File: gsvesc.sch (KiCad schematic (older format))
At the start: 29 parts, among them J1 Conn_01x06, J13 Conn_01x02, J2 Conn_01x06, J3 Conn_01x06, J4 Conn_01x05, J5 Conn_01x03, J6 USB_B_Mini, J7 BAT+, J8 BAT-, U17 TMP100NA_250

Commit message: fertig gerouted
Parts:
- added R37, R40: R, Resistor_SMD:R_0805_2012Metric, symbol Device:R
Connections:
- net MCU/I2C1_SCL: now also R40.2
- net MCU/I2C1_SDA: now also R37.2
- net VCC: now also R37.1, R40.1
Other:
- moved on the sheet: U17
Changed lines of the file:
@@
 L gsvesc:TMP100NA_250 U17
 U 1 1 5EB0793D
-P 5250 4650
-F 0 "U17" H 6050 5137 60  0000 C CNN
-F 1 "TMP100NA_250" H 6050 5031 60  0000 C CNN
-F 2 "gsvesc:TMP100NA_250" H 6050 4990 60  0001 C CNN
-F 3 "" H 5250 4650 60  0000 C CNN
-	1    5250 4650
+P 7600 5500
+F 0 "U17" H 8400 5987 60  0000 C CNN
+F 1 "TMP100NA_250" H 8400 5881 60  0000 C CNN
+F 2 "gsvesc:TMP100NA_250" H 8400 5840 60  0001 C CNN
+F 3 "" H 7600 5500 60  0000 C CNN
+	1    7600 5500
 	1    0    0    -1
 $EndComp
-Wire Wire Line
-	4600 4600 4750 4600
-Wire Wire Line
-	4750 4600 4750 4450
-Wire Wire Line
-	4750 4450 5250 4450
-Wire Wire Line
-	4600 4700 4800 4700
-Wire Wire Line
-	4800 4700 4800 4550
-Wire Wire Line
-	4800 4550 5250 4550
 $Comp
 L power:VCC #PWR0159
 U 1 1 5EB10F14
-P 5250 4700
-F 0 "#PWR0159" H 5250 4550 50  0001 C CNN
-F 1 "VCC" V 5268 4827 50  0000 L CNN
-F 2 "" H 5250 4700 50  0001 C CNN
-F 3 "" H 5250 4700 50  0001 C CNN
-	1    5250 4700
+P 7600 5550
+F 0 "#PWR0159" H 7600 5400 50  0001 C CNN
+F 1 "VCC" V 7618 5677 50  0000 L CNN
+F 2 "" H 7600 5550 50  0001 C CNN
+F 3 "" H 7600 5550 50  0001 C CNN
+	1    7600 5550
 	0    -1   -1   0
 $EndComp
@@
 L power:GND #PWR0160
 U 1 1 5EB11007
-P 6400 4700
-F 0 "#PWR0160" H 6400 4450 50  0001 C CNN
-F 1 "GND" H 6405 4527 50  0000 C CNN
-F 2 "" H 6400 4700 50  0001 C CNN
-F 3 "" H 6400 4700 50  0001 C CNN
-	1    6400 4700
+P 8750 5550
+F 0 "#PWR0160" H 8750 5300 50  0001 C CNN
+F 1 "GND" H 8755 5377 50  0000 C CNN
+F 2 "" H 8750 5550 50  0001 C CNN
+F 3 "" H 8750 5550 50  0001 C CNN
+	1    8750 5550
 	1    0    0    -1
 $EndComp
+Wire Wire Line
+	6850 4700 6850 5400
+Wire Wire Line
+	7000 4600 7000 5300
+Wire Wire Line
+	7000 5300 7400 5300
+Wire Wire Line
+	4600 4700 6850 4700
+Wire Wire Line
+	4600 4600 7000 4600
+$Comp
+L Device:R R37
+U 1 1 5EB13175
+P 7150 5050
+F 0 "R37" H 7220 5096 50  0000 L CNN
+F 1 "R" H 7220 5005 50  0000 L CNN
+F 2 "Resistor_SMD:R_0805_2012Metric" V 7080 5050 50  0001 C CNN
+F 3 "~" H 7150 5050 50  0001 C CNN
+	1    7150 5050
+	1    0    0    -1
+$EndComp
+$Comp
+L Device:R R40
+U 1 1 5EB132CF
+P 7400 5050
+F 0 "R40" H 7470 5096 50  0000 L CNN
+F 1 "R" H 7470 5005 50  0000 L CNN
+F 2 "Resistor_SMD:R_0805_2012Metric" V 7330 5050 50  0001 C CNN
+F 3 "~" H 7400 5050 50  0001 C CNN
+	1    7400 5050
+	1    0    0    -1
+$EndComp
+Wire Wire Line
+	7400 5200 7400 5300
+Connection ~ 7400 5300
+Wire Wire Line
+	7400 5300 7600 5300
+Wire Wire Line
+	7150 5200 7150 5400
+Wire Wire Line
+	6850 5400 7150 5400
+Connection ~ 7150 5400
+Wire Wire Line
+	7150 5400 7600 5400
+Wire Wire Line
+	7150 4900 7150 4800
+Wire Wire Line
+	7150 4800 7400 4800
+Wire Wire Line
+	7400 4800 7400 4900
+$Comp
+L power:VCC #PWR0161
+U 1 1 5EB25A1D
+P 7150 4800
+F 0 "#PWR0161" H 7150 4650 50  0001 C CNN
+F 1 "VCC" V 7168 4927 50  0000 L CNN
+F 2 "" H 7150 4800 50  0001 C CNN
+F 3 "" H 7150 4800 50  0001 C CNN
+	1    7150 4800
+	1    0    0    -1
+$EndComp
+Connection ~ 7150 4800
 $EndSCHEMATC

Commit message: Ready for JLC
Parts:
- R37, R40: value R -> 10k0
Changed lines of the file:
@@
 P 7150 5050
 F 0 "R37" H 7220 5096 50  0000 L CNN
-F 1 "R" H 7220 5005 50  0000 L CNN
+F 1 "10k0" H 7220 5005 50  0000 L CNN
 F 2 "Resistor_SMD:R_0805_2012Metric" V 7080 5050 50  0001 C CNN
 F 3 "~" H 7150 5050 50  0001 C CNN
@@
 P 7400 5050
 F 0 "R40" H 7470 5096 50  0000 L CNN
-F 1 "R" H 7470 5005 50  0000 L CNN
+F 1 "10k0" H 7470 5005 50  0000 L CNN
 F 2 "Resistor_SMD:R_0805_2012Metric" V 7330 5050 50  0001 C CNN
 F 3 "~" H 7400 5050 50  0001 C CNN

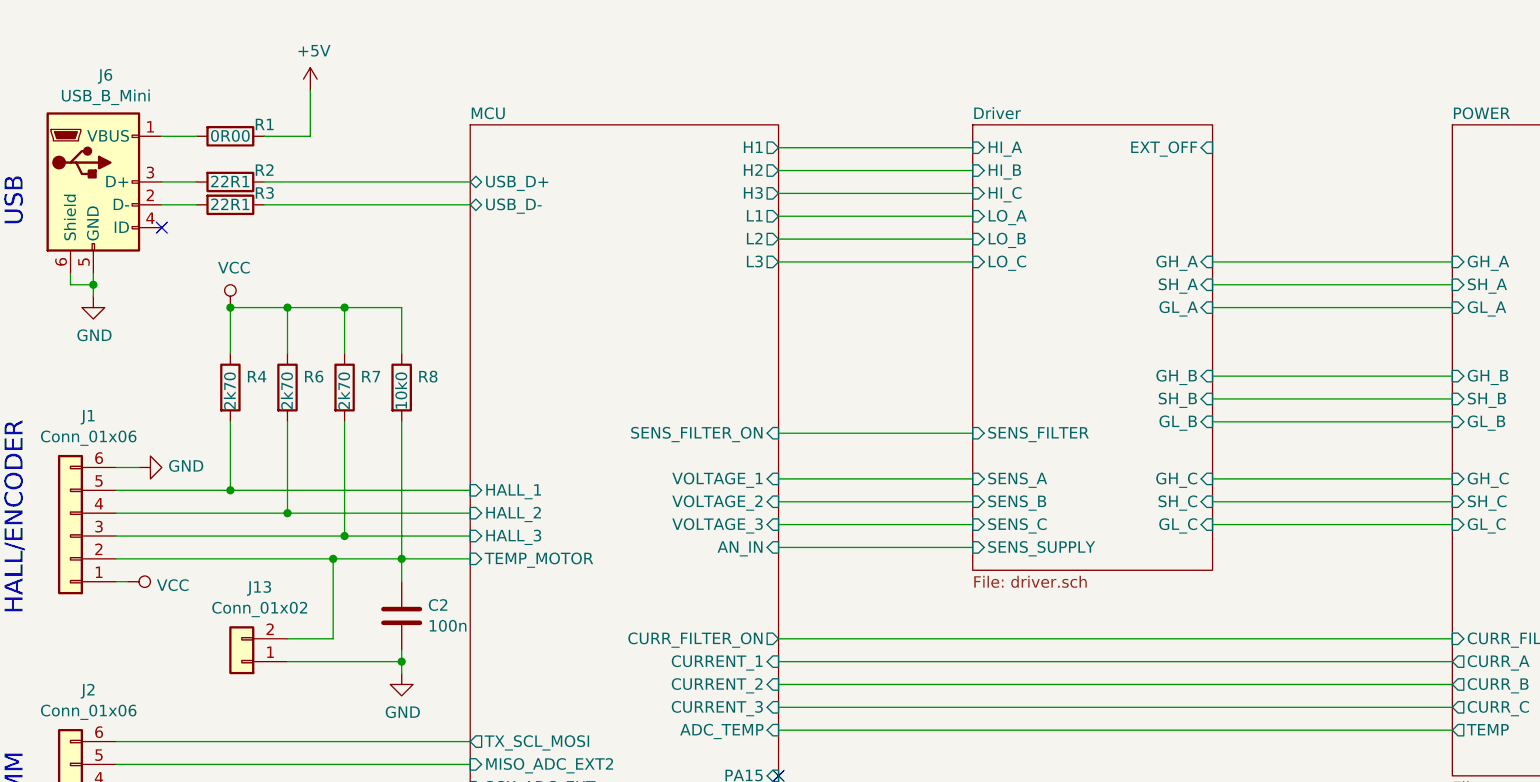
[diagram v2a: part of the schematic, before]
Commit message: some bug fixes for next pcb-run
- Add JST connector for Motor Temp
- Remove USB 5V
- add correct footprint for D8,9,10
- add JST connector for external off
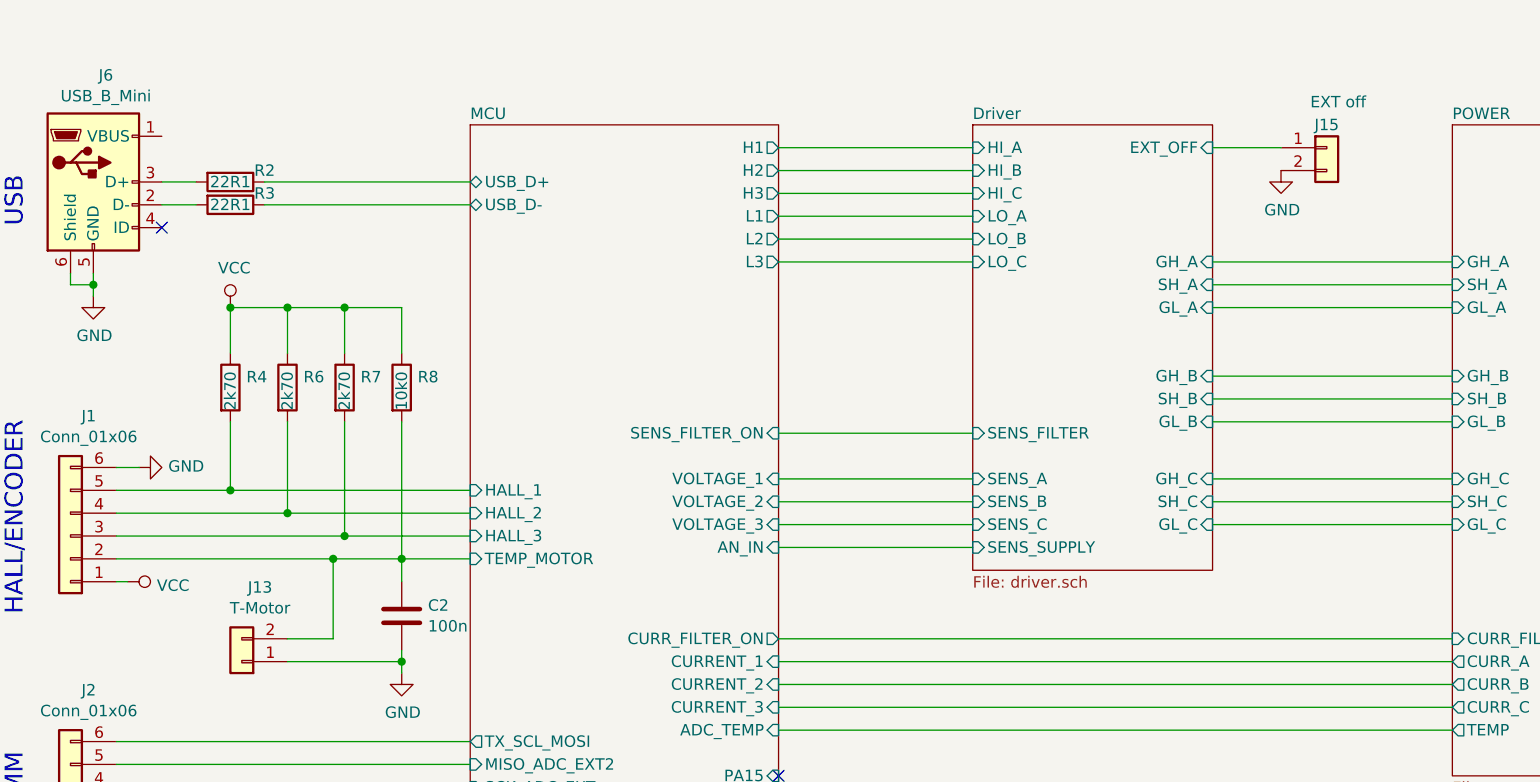
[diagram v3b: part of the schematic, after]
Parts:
- removed R1: 0R00, Resistor_SMD:R_0805_2012Metric, symbol Device:R
- added J15: EXT off, Connector_JST:JST_SH_BM02B-SRSS-TB_1x02-1MP_P1.00mm_Vertical, symbol Connector_Generic:Conn_01x02
- J13: value Conn_01x02 -> T-Motor; footprint gsvesc:2pad_smd_testpin -> Connector_JST:JST_SH_BM02B-SRSS-TB_1x02-1MP_P1.00mm_Vertical
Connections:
- net Driver/EXT_OFF: now also J15.1 (Pin_1)
- net GND: now also J15.2 (Pin_2)
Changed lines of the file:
@@
 	1600 2200 1600 2150
-$Comp
-L Device:R R1
-U 1 1 5BE878C2
-P 2200 1500
-F 0 "R1" V 2150 1650 50  0000 C CNN
-F 1 "0R00" V 2200 1500 50  0000 C CNN
-F 2 "Resistor_SMD:R_0805_2012Metric" V 2130 1500 50  0001 C CNN
-F 3 "~" H 2200 1500 50  0001 C CNN
-	1    2200 1500
-	0    1    1    0
-$EndComp
 $Comp
 L Device:R R2
@@
 	0    1    1    0
 $EndComp
-Wire Wire Line
-	1900 1500 2050 1500
-Wire Wire Line
-	2350 1500 2550 1500
-Wire Wire Line
-	2550 1500 2550 1300
 Wire Wire Line
 	1500 2100 1500 2150
@@
 F6 "GPIO3" I L 5200 5200 50
 $EndSheet
-$Comp
-L power:+5V #PWR013
-U 1 1 5BEB4C48
-P 2550 1300
-F 0 "#PWR013" H 2550 1150 50  0001 C CNN
-F 1 "+5V" H 2565 1473 50  0000 C CNN
-F 2 "" H 2550 1300 50  0001 C CNN
-F 3 "" H 2550 1300 50  0001 C CNN
-	1    2550 1300
-	1    0    0    -1
-$EndComp
 Wire Wire Line
 	4600 1550 5450 1550
@@
 P 2250 3800
 F 0 "J13" H 2170 3475 50  0000 C CNN
-F 1 "Conn_01x02" H 2170 3566 50  0000 C CNN
-F 2 "gsvesc:2pad_smd_testpin" H 2250 3800 50  0001 C CNN
+F 1 "T-Motor" H 2170 3566 50  0000 C CNN
+F 2 "Connector_JST:JST_SH_BM02B-SRSS-TB_1x02-1MP_P1.00mm_Vertical" H 2250 3800 50  0001 C CNN
 F 3 "~" H 2250 3800 50  0001 C CNN
 	1    2250 3800
@@
 $EndComp
 Connection ~ 7150 4800
+$Comp
+L Connector_Generic:Conn_01x02 J15
+U 1 1 5ECFB072
+P 7000 1550
+F 0 "J15" H 7000 1650 50  0000 C CNN
+F 1 "EXT off" H 7050 1750 50  0000 C CNN
+F 2 "Connector_JST:JST_SH_BM02B-SRSS-TB_1x02-1MP_P1.00mm_Vertical" H 7000 1550 50  0001 C CNN
+F 3 "~" H 7000 1550 50  0001 C CNN
+	1    7000 1550
+	1    0    0    -1
+$EndComp
+Wire Wire Line
+	6500 1550 6800 1550
+$Comp
+L power:GND #PWR0154
+U 1 1 5ECFFD27
+P 6800 1650
+F 0 "#PWR0154" H 6800 1400 50  0001 C CNN
+F 1 "GND" H 6805 1477 50  0000 C CNN
+F 2 "" H 6800 1650 50  0001 C CNN
+F 3 "" H 6800 1650 50  0001 C CNN
+	1    6800 1650
+	1    0    0    -1
+$EndComp
 $EndSCHEMATC

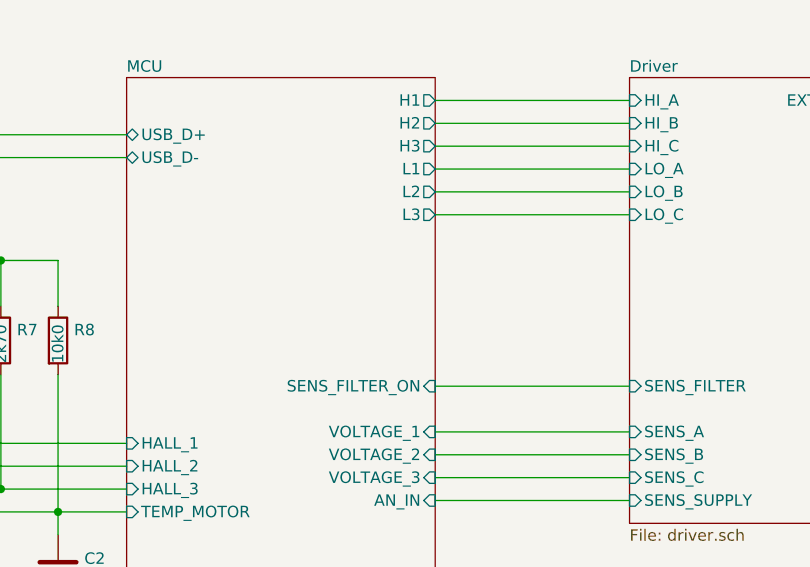
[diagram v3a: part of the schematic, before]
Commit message: BUG Fixes, see BUGS.txt
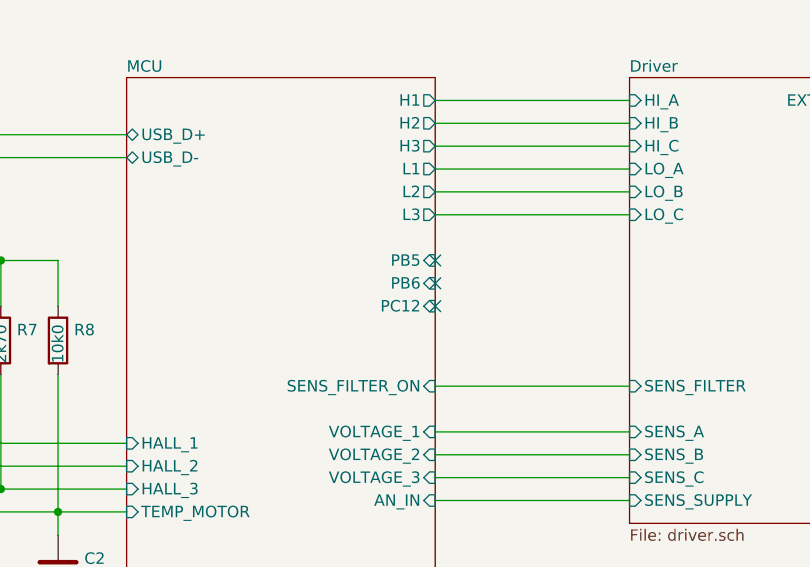
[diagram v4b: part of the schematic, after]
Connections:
- no-connect marks 3 -> 6
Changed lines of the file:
@@
 F45 "I2C1_SCL" I R 4600 4600 50
 F46 "I2C1_SDA" I R 4600 4700 50
+F47 "PB5" I R 4600 2250 50
+F48 "PB6" I R 4600 2350 50
+F49 "PC12" I R 4600 2450 50
 $EndSheet
 $Sheet
@@
 	1    0    0    -1
 $EndComp
+NoConn ~ 4600 2250
+NoConn ~ 4600 2350
+NoConn ~ 4600 2450
 $EndSCHEMATC

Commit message: bug fixing
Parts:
- removed J15: EXT off, Connector_JST:JST_SH_BM02B-SRSS-TB_1x02-1MP_P1.00mm_Vertical, symbol Connector_Generic:Conn_01x02
- added J15: EXT_OFF, Connector_JST:JST_SH_BM06B-SRSS-TB_1x06-1MP_P1.00mm_Vertical, symbol Connector_Generic:Conn_01x06
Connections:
- net +12V: now also J15.2 (Pin_2)
- net Driver/EXT_OFF: now also J15.4 (Pin_4)
- net GND: now also J15.6 (Pin_6)
- net VBAT: now also J15.1 (Pin_1)
- net VCC: now also J15.3 (Pin_3)
- new net Driver/EXT_OFF_DIRECT: J15.5 (Pin_5)
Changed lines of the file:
@@
 F21 "SENS_A" I L 5450 3000 50
 F22 "EXT_OFF" I R 6500 1550 50
+F23 "EXT_OFF_DIRECT" I R 6500 1650 50
 $EndSheet
 Wire Wire Line
@@
 Connection ~ 7150 4800
 $Comp
-L Connector_Generic:Conn_01x02 J15
-U 1 1 5ECFB072
-P 7000 1550
-F 0 "J15" H 7000 1650 50  0000 C CNN
-F 1 "EXT off" H 7050 1750 50  0000 C CNN
-F 2 "Connector_JST:JST_SH_BM02B-SRSS-TB_1x02-1MP_P1.00mm_Vertical" H 7000 1550 50  0001 C CNN
-F 3 "~" H 7000 1550 50  0001 C CNN
-	1    7000 1550
-	1    0    0    -1
-$EndComp
-Wire Wire Line
-	6500 1550 6800 1550
-$Comp
 L power:GND #PWR0154
 U 1 1 5ECFFD27
-P 6800 1650
-F 0 "#PWR0154" H 6800 1400 50  0001 C CNN
-F 1 "GND" H 6805 1477 50  0000 C CNN
-F 2 "" H 6800 1650 50  0001 C CNN
-F 3 "" H 6800 1650 50  0001 C CNN
-	1    6800 1650
+P 6950 1750
+F 0 "#PWR0154" H 6950 1500 50  0001 C CNN
+F 1 "GND" H 6955 1577 50  0000 C CNN
+F 2 "" H 6950 1750 50  0001 C CNN
+F 3 "" H 6950 1750 50  0001 C CNN
+	1    6950 1750
 	1    0    0    -1
 $EndComp
@@
 NoConn ~ 4600 2350
 NoConn ~ 4600 2450
+$Comp
+L power:VCC #PWR0162
+U 1 1 5ECFCDBF
+P 6950 1450
+F 0 "#PWR0162" H 6950 1300 50  0001 C CNN
+F 1 "VCC" V 6968 1577 50  0000 L CNN
+F 2 "" H 6950 1450 50  0001 C CNN
+F 3 "" H 6950 1450 50  0001 C CNN
+	1    6950 1450
+	0    -1   -1   0
+$EndComp
+Wire Wire Line
+	6500 1550 6950 1550
+$Comp
+L Connector_Generic:Conn_01x06 J15
+U 1 1 5ED44562
+P 7150 1450
+F 0 "J15" H 7100 1750 50  0000 C CNN
+F 1 "EXT_OFF" H 7150 1850 50  0000 C CNN
+F 2 "Connector_JST:JST_SH_BM06B-SRSS-TB_1x06-1MP_P1.00mm_Vertical" H 7150 1450 50  0001 C CNN
+F 3 "~" H 7150 1450 50  0001 C CNN
+	1    7150 1450
+	1    0    0    -1
+$EndComp
+Wire Wire Line
+	6500 1650 6950 1650
+$Comp
+L power:+12V #PWR0165
+U 1 1 5ED6AA00
+P 6950 1350
+F 0 "#PWR0165" H 6950 1200 50  0001 C CNN
+F 1 "+12V" V 6965 1478 50  0000 L CNN
+F 2 "" H 6950 1350 50  0001 C CNN
+F 3 "" H 6950 1350 50  0001 C CNN
+	1    6950 1350
+	0    -1   -1   0
+$EndComp
+Text GLabel 6950 1250 0    50   Input ~ 0
+VBAT
 $EndSCHEMATC

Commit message: add PDF
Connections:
- net Driver/EXT_OFF renamed Driver/EN_3V3
- net Driver/EXT_OFF_DIRECT renamed Driver/EN_12V
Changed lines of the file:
@@
 F20 "SENS_B" I L 5450 3100 50
 F21 "SENS_A" I L 5450 3000 50
-F22 "EXT_OFF" I R 6500 1550 50
-F23 "EXT_OFF_DIRECT" I R 6500 1650 50
+F22 "EN_3V3" I R 6500 1550 50
+F23 "EN_12V" I R 6500 1650 50
 $EndSheet
 Wire Wire Line
@@
 NoConn ~ 4600 2350
 NoConn ~ 4600 2450
+Wire Wire Line
+	6500 1550 6950 1550
+$Comp
+L Connector_Generic:Conn_01x06 J15
+U 1 1 5ED44562
+P 7150 1450
+F 0 "J15" H 7100 1750 50  0000 C CNN
+F 1 "EXT_OFF" H 7150 1850 50  0000 C CNN
+F 2 "Connector_JST:JST_SH_BM06B-SRSS-TB_1x06-1MP_P1.00mm_Vertical" H 7150 1450 50  0001 C CNN
+F 3 "~" H 7150 1450 50  0001 C CNN
+	1    7150 1450
+	1    0    0    -1
+$EndComp
+Wire Wire Line
+	6500 1650 6950 1650
+Text GLabel 6950 1250 0    50   Input ~ 0
+VBAT
+$Comp
+L power:+12V #PWR0165
+U 1 1 5ED6AA00
+P 6950 1350
+F 0 "#PWR0165" H 6950 1200 50  0001 C CNN
+F 1 "+12V" V 6965 1478 50  0000 L CNN
+F 2 "" H 6950 1350 50  0001 C CNN
+F 3 "" H 6950 1350 50  0001 C CNN
+	1    6950 1350
+	0    -1   -1   0
+$EndComp
 $Comp
 L power:VCC #PWR0162
@@
 	0    -1   -1   0
 $EndComp
-Wire Wire Line
-	6500 1550 6950 1550
-$Comp
-L Connector_Generic:Conn_01x06 J15
-U 1 1 5ED44562
-P 7150 1450
-F 0 "J15" H 7100 1750 50  0000 C CNN
-F 1 "EXT_OFF" H 7150 1850 50  0000 C CNN
-F 2 "Connector_JST:JST_SH_BM06B-SRSS-TB_1x06-1MP_P1.00mm_Vertical" H 7150 1450 50  0001 C CNN
-F 3 "~" H 7150 1450 50  0001 C CNN
-	1    7150 1450
-	1    0    0    -1
-$EndComp
-Wire Wire Line
-	6500 1650 6950 1650
-$Comp
-L power:+12V #PWR0165
-U 1 1 5ED6AA00
-P 6950 1350
-F 0 "#PWR0165" H 6950 1200 50  0001 C CNN
-F 1 "+12V" V 6965 1478 50  0000 L CNN
-F 2 "" H 6950 1350 50  0001 C CNN
-F 3 "" H 6950 1350 50  0001 C CNN
-	1    6950 1350
-	0    -1   -1   0
-$EndComp
-Text GLabel 6950 1250 0    50   Input ~ 0
-VBAT
 $EndSCHEMATC

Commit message: hw 4 freeze
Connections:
- net GND: now also U17.3 (ADD1)
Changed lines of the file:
@@
 	0    -1   -1   0
 $EndComp
+Wire Wire Line
+	8750 5400 8750 5550
+Connection ~ 8750 5550
 $EndSCHEMATC

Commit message: temp
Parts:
- added C53, C54, C55, C56: 330u, Capacitor_SMD:CP_Elec_10x12.5, symbol Device:CP
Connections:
- net GND: now also C53.2, C54.2, C55.2, C56.2
- net VBAT: now also C53.1, C54.1, C55.1, C56.1
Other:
- moved on the sheet: J7, J8
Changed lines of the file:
@@
 L Connector_Generic:Conn_01x01 J7
 U 1 1 5C0450D0
-P 9950 1550
-F 0 "J7" H 10030 1592 50  0000 L CNN
-F 1 "BAT+" H 10030 1501 50  0000 L CNN
-F 2 "gsvesc:TestPoint_Pad_5.0x5.0mm" H 9950 1550 50  0001 C CNN
-F 3 "~" H 9950 1550 50  0001 C CNN
-	1    9950 1550
+P 10850 1350
+F 0 "J7" H 10930 1392 50  0000 L CNN
+F 1 "BAT+" H 10930 1301 50  0000 L CNN
+F 2 "gsvesc:TestPoint_Pad_5.0x5.0mm" H 10850 1350 50  0001 C CNN
+F 3 "~" H 10850 1350 50  0001 C CNN
+	1    10850 1350
 	1    0    0    -1
 $EndComp
@@
 L Connector_Generic:Conn_01x01 J8
 U 1 1 5C045122
-P 9950 1900
-F 0 "J8" H 10030 1942 50  0000 L CNN
-F 1 "BAT-" H 10030 1851 50  0000 L CNN
-F 2 "gsvesc:TestPoint_Pad_5.0x5.0mm" H 9950 1900 50  0001 C CNN
-F 3 "~" H 9950 1900 50  0001 C CNN
-	1    9950 1900
-	1    0    0    -1
-$EndComp
-Wire Wire Line
-	9750 1900 9550 1900
+P 10850 1900
+F 0 "J8" H 10930 1942 50  0000 L CNN
+F 1 "BAT-" H 10930 1851 50  0000 L CNN
+F 2 "gsvesc:TestPoint_Pad_5.0x5.0mm" H 10850 1900 50  0001 C CNN
+F 3 "~" H 10850 1900 50  0001 C CNN
+	1    10850 1900
+	1    0    0    -1
+$EndComp
 $Comp
 L power:GND #PWR019
@@
 L power:PWR_FLAG #FLG0102
 U 1 1 5C34D8D2
-P 9550 1550
-F 0 "#FLG0102" H 9550 1625 50  0001 C CNN
-F 1 "PWR_FLAG" V 9550 1678 50  0000 L CNN
-F 2 "" H 9550 1550 50  0001 C CNN
-F 3 "~" H 9550 1550 50  0001 C CNN
-	1    9550 1550
+P 9550 1350
+F 0 "#FLG0102" H 9550 1425 50  0001 C CNN
+F 1 "PWR_FLAG" V 9550 1478 50  0000 L CNN
+F 2 "" H 9550 1350 50  0001 C CNN
+F 3 "~" H 9550 1350 50  0001 C CNN
+	1    9550 1350
 	1    0    0    -1
 $EndComp
@@
 F15 "CURR_FILTER" I L 7550 3700 50
 $EndSheet
-Wire Wire Line
-	9550 1550 9750 1550
-Text GLabel 9350 1550 0    50   Input ~ 0
+Text GLabel 9350 1350 0    50   Input ~ 0
 VBAT
-Wire Wire Line
-	9550 1550 9350 1550
-Connection ~ 9550 1550
 Wire Wire Line
 	9550 1900 9550 2000
@@
 	0    -1   -1   0
 $EndComp
-Connection ~ 9550 1900
 Wire Wire Line
 	9550 2650 9950 2650
@@
 	8750 5400 8750 5550
 Connection ~ 8750 5550
+Connection ~ 9550 1900
+$Comp
+L Device:CP C53
+U 1 1 5F3842E8
+P 9650 1650
+F 0 "C53" H 9768 1696 50  0000 L CNN
+F 1 "330u" H 9768 1605 50  0000 L CNN
+F 2 "Capacitor_SMD:CP_Elec_10x12.5" H 9688 1500 50  0001 C CNN
+F 3 "~" H 9650 1650 50  0001 C CNN
+	1    9650 1650
+	1    0    0    -1
+$EndComp
+$Comp
+L Device:CP C54
+U 1 1 5F3843DA
+P 9900 1650
+F 0 "C54" H 10018 1696 50  0000 L CNN
+F 1 "330u" H 10018 1605 50  0000 L CNN
+F 2 "Capacitor_SMD:CP_Elec_10x12.5" H 9938 1500 50  0001 C CNN
+F 3 "~" H 9900 1650 50  0001 C CNN
+	1    9900 1650
+	1    0    0    -1
+$EndComp
+Wire Wire Line
+	9650 1500 9650 1350
+Connection ~ 9650 1350
+Wire Wire Line
+	9650 1350 9900 1350
+Wire Wire Line
+	9650 1800 9650 1900
+Connection ~ 9650 1900
+Wire Wire Line
+	9650 1900 9550 1900
+Wire Wire Line
+	9900 1800 9900 1900
+Wire Wire Line
+	9900 1500 9900 1350
+Wire Wire Line
+	9550 1350 9650 1350
+Wire Wire Line
+	9550 1900 9450 1900
+Wire Wire Line
+	9350 1350 9550 1350
+Connection ~ 9900 1350
+Connection ~ 9900 1900
+Wire Wire Line
+	9900 1900 9650 1900
+Connection ~ 9550 1350
+$Comp
+L Device:CP C55
+U 1 1 5F3B3A44
+P 10150 1650
+F 0 "C55" H 10268 1696 50  0000 L CNN
+F 1 "330u" H 10268 1605 50  0000 L CNN
+F 2 "Capacitor_SMD:CP_Elec_10x12.5" H 10188 1500 50  0001 C CNN
+F 3 "~" H 10150 1650 50  0001 C CNN
+	1    10150 1650
+	1    0    0    -1
+$EndComp
+$Comp
+L Device:CP C56
+U 1 1 5F3B3A4A
+P 10400 1650
+F 0 "C56" H 10518 1696 50  0000 L CNN
+F 1 "330u" H 10518 1605 50  0000 L CNN
+F 2 "Capacitor_SMD:CP_Elec_10x12.5" H 10438 1500 50  0001 C CNN
+F 3 "~" H 10400 1650 50  0001 C CNN
+	1    10400 1650
+	1    0    0    -1
+$EndComp
+Wire Wire Line
+	10150 1500 10150 1350
+Connection ~ 10150 1350
+Wire Wire Line
+	10150 1350 10400 1350
+Wire Wire Line
+	10150 1800 10150 1900
+Connection ~ 10150 1900
+Wire Wire Line
+	10400 1800 10400 1900
+Wire Wire Line
+	10400 1500 10400 1350
+Connection ~ 10400 1350
+Connection ~ 10400 1900
+Wire Wire Line
+	10400 1900 10150 1900
+Wire Wire Line
+	10400 1350 10650 1350
+Wire Wire Line
+	10400 1900 10650 1900
+Wire Wire Line
+	10050 1350 10150 1350
+Wire Wire Line
+	10050 1900 10150 1900
+Wire Wire Line
+	9900 1350 10150 1350
+Wire Wire Line
+	9900 1900 10150 1900
 $EndSCHEMATC
